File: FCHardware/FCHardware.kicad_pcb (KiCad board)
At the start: 2 copper layers, 39 parts, among them J1 JST-8pin, J3 USB_C_Receptacle_USB2.0_16P, SW3 SW_Push, U2 MPU-6050, U4 TPSM63603, U8 ESP32-S3-MINI-1U, U9 USBLC6-2SC6

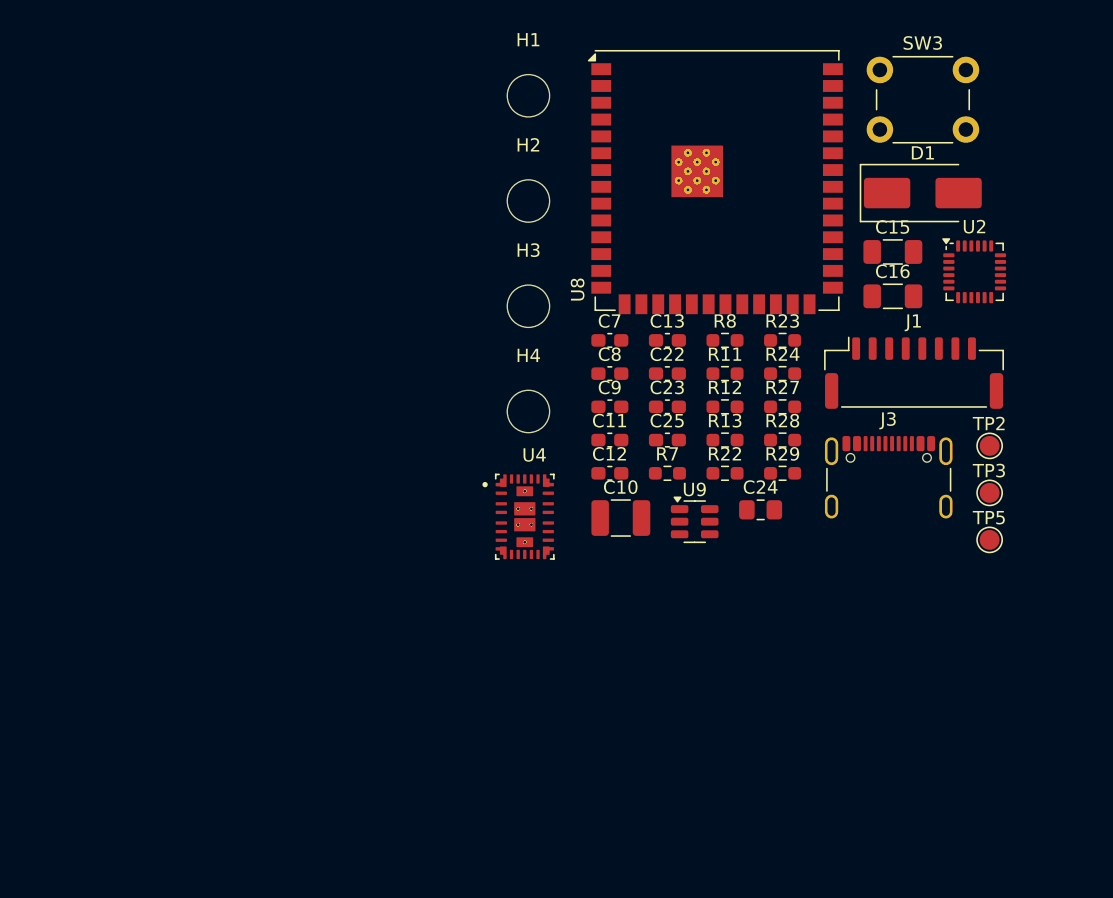
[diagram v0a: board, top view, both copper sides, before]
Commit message: Created basic component placement
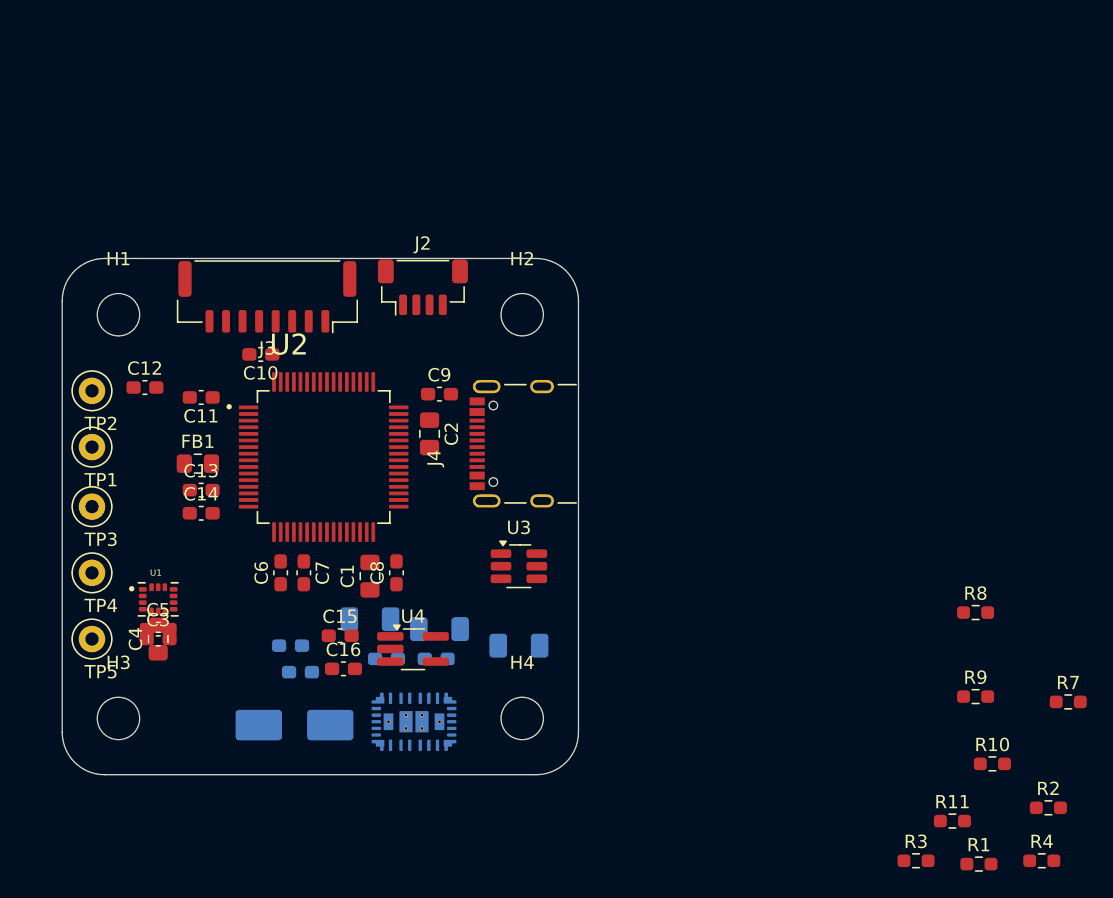
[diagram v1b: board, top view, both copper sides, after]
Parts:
- removed C24: 10u, Capacitor_SMD:C_0805_2012Metric_Pad1.18x1.45mm_HandSolder
- removed C25: 100n, Capacitor_SMD:C_0603_1608Metric_Pad1.08x0.95mm_HandSolder
- removed J1: JST-8pin, Connector_JST:JST_GH_SM08B-GHS-TB_1x08-1MP_P1.25mm_Horizontal
- removed R12: 23.2k, Resistor_SMD:R_0603_1608Metric_Pad0.98x0.95mm_HandSolder
- removed R13, R24, R27: 10k, Resistor_SMD:R_0603_1608Metric_Pad0.98x0.95mm_HandSolder
- removed R22: 510k, Resistor_SMD:R_0603_1608Metric_Pad0.98x0.95mm_HandSolder
- removed R23: 68k, Resistor_SMD:R_0603_1608Metric_Pad0.98x0.95mm_HandSolder
- removed R28, R29: 5k1 +-5%, Resistor_SMD:R_0603_1608Metric_Pad0.98x0.95mm_HandSolder
- removed SW3: SW_Push, Button_Switch_THT:SW_PUSH_6mm
- removed U8: ESP32-S3-MINI-1U, RF_Module:ESP32-S3-WROOM-1U
- removed U9: USBLC6-2SC6, Package_TO_SOT_SMD:SOT-23-6
- added C1: 2u2, Capacitor_SMD:C_0805_2012Metric_Pad1.18x1.45mm_HandSolder, F.Cu at (103.5, 104.2)
- added C14: 1u, Capacitor_SMD:C_0603_1608Metric_Pad1.08x0.95mm_HandSolder, F.Cu at (90.8, 99.5)
- added C17: 680n, Capacitor_SMD:C_0603_1608Metric_Pad1.08x0.95mm_HandSolder, B.Cu at (98.2, 111.5)
- added C18: 100n, Capacitor_SMD:C_0603_1608Metric_Pad1.08x0.95mm_HandSolder, B.Cu at (97.5, 109.5)
- added C19: 22u, Capacitor_SMD:C_1206_3216Metric_Pad1.33x1.80mm_HandSolder, B.Cu at (103.5, 107.5)
- added C2: 2u2, Capacitor_SMD:C_0805_2012Metric_Pad1.18x1.45mm_HandSolder, F.Cu at (108.0, 93.5)
- added C20: 1u, Capacitor_SMD:C_0603_1608Metric_Pad1.08x0.95mm_HandSolder, B.Cu at (104.8, 110.5)
- added C21: 22u, Capacitor_SMD:C_1206_3216Metric_Pad1.33x1.80mm_HandSolder, B.Cu at (108.8, 108.2)
- added C3: 0u1, Capacitor_SMD:C_0603_1608Metric_Pad1.08x0.95mm_HandSolder, F.Cu at (87.5, 109.0)
- added C4: 2u2, Capacitor_SMD:C_0805_2012Metric_Pad1.18x1.45mm_HandSolder, F.Cu at (87.5, 109.0)
- added C5: 0u1, Capacitor_SMD:C_0603_1608Metric_Pad1.08x0.95mm_HandSolder, F.Cu at (87.5, 108.2)
- added C6: 100n, Capacitor_SMD:C_0603_1608Metric_Pad1.08x0.95mm_HandSolder, F.Cu at (96.8, 104.0)
- added FB1: 1kOhm 100Mhz, Inductor_SMD:L_0805_2012Metric_Pad1.15x1.40mm_HandSolder, F.Cu at (90.5, 95.8)
- added J2: JST-4pin, Connector_JST:JST_SH_BM04B-SRSS-TB_1x04-1MP_P1.00mm_Vertical, F.Cu at (107.5, 82.4)
- added J4: UJ20-C-H-G-SMT-2A-P16-TR, FCFootprints:SAMESKY_UJ20-C-H-G-SMT-2A-P16-TR, F.Cu at (116.5, 94.2)
- added R1: 68k, Resistor_SMD:R_0603_1608Metric_Pad0.98x0.95mm_HandSolder, F.Cu at (149.5, 126.0)
- added R10: 5k1, Resistor_SMD:R_0603_1608Metric_Pad0.98x0.95mm_HandSolder, F.Cu at (150.5, 118.4)
- added R2: 510k, Resistor_SMD:R_0603_1608Metric_Pad0.98x0.95mm_HandSolder, F.Cu at (154.8, 121.8)
- added R3: 10k, Resistor_SMD:R_0603_1608Metric_Pad0.98x0.95mm_HandSolder, F.Cu at (144.8, 125.8)
- added R4: 10k, Resistor_SMD:R_0603_1608Metric_Pad0.98x0.95mm_HandSolder, F.Cu at (154.2, 125.8)
- added R9: 10k, Resistor_SMD:R_0603_1608Metric_Pad0.98x0.95mm_HandSolder, F.Cu at (149.2, 113.3)
- added TP1: BootTestPoint, TestPoint:TestPoint_Loop_D1.80mm_Drill1.0mm_Beaded, F.Cu at (82.5, 94.5)
- added TP4: 5VTestPoint, TestPoint:TestPoint_Loop_D1.80mm_Drill1.0mm_Beaded, F.Cu at (82.5, 104.0)
- added U1: ICM-42688-P, FCFootprints:PQFN50P300X250X97-14N, F.Cu at (87.5, 106.0)
- added U3: USBLC6-2SC6, Package_TO_SOT_SMD:SOT-23-6_Handsoldering, F.Cu at (114.8, 103.5)
- added U5: TPSM63603, FCFootprints:CONV_TPSM63603EXTRDHR, B.Cu at (106.8, 115.2)
- C10: value 680n -> 100n; footprint Capacitor_SMD:C_1210_3225Metric_Pad1.33x2.70mm_HandSolder -> Capacitor_SMD:C_0603_1608Metric_Pad1.08x0.95mm_HandSolder
- C12, C7: value 1u -> 100n
- C13: value 100n -> 10n
- C15, C16: value 22u -> 1u; footprint Capacitor_SMD:C_1206_3216Metric_Pad1.33x1.80mm_HandSolder -> Capacitor_SMD:C_0603_1608Metric_Pad1.08x0.95mm_HandSolder
- C22, D1: moved to B.Cu
- C23: value 100n -> 22u; footprint Capacitor_SMD:C_0603_1608Metric_Pad1.08x0.95mm_HandSolder -> Capacitor_SMD:C_1206_3216Metric_Pad1.33x1.80mm_HandSolder; moved to B.Cu
- C9: value 2n2 -> 100n
- J3: value USB_C_Receptacle_USB2.0_16P -> JST-8pin; footprint Connector_USB:USB_C_Receptacle_GCT_USB4105-xx-A_16P_TopMnt_Horizontal -> Connector_Molex:Molex_CLIK-Mate_502386-0870_1x08-1MP_P1.25mm_Horizontal
- R11: value 27.4k -> 5k1
- R7: value 2k2 -> 13k
- R8: value 2k2 -> 40.2k
- TP2: value GNDTestPoint -> ResetTestPoint; footprint TestPoint:TestPoint_Pad_D1.5mm -> TestPoint:TestPoint_Loop_D1.80mm_Drill1.0mm_Beaded
- TP3: value 3V3TestPoint -> GNDTestPoint; footprint TestPoint:TestPoint_Pad_D1.5mm -> TestPoint:TestPoint_Loop_D1.80mm_Drill1.0mm_Beaded
- TP5: value ENTestPoint -> 3V3TestPoint; footprint TestPoint:TestPoint_Pad_D1.5mm -> TestPoint:TestPoint_Loop_D1.80mm_Drill1.0mm_Beaded
- U2: value MPU-6050 -> STM32F405RGTx; footprint Sensor_Motion:InvenSense_QFN-24_4x4mm_P0.5mm -> FCFootprints:QFP50P1200X1200X160-64N
- U4: value TPSM63603 -> AP2112K-3.3; footprint FCFootprints:CONV_TPSM63603EXTRDHR -> Package_TO_SOT_SMD:TSOT-23-5_HandSoldering
- moved TP5 68.2 mm to (82.5, 109.0)
- moved TP2 67.9 mm to (82.5, 90.2)
- moved TP3 67.8 mm to (82.5, 99.0)
- moved D1 62.2 mm to (97.8, 115.5), turned to 180 degrees
- moved U2 51.1 mm to (100.0, 95.2)
- moved C15 50.8 mm to (101.2, 108.8)
- moved C16 50.1 mm to (101.5, 111.2)
- moved J3 49.2 mm to (95.8, 83.2), turned to 180 degrees
- moved H3 43.9 mm to (84.5, 115.0)
- moved R11 37.9 mm to (147.5, 122.8)
- moved C13 37.0 mm to (90.8, 97.8)
- moved C12 35.7 mm to (86.5, 90.0)
- moved H1 35.1 mm to (84.5, 84.5)
- moved R7 34.9 mm to (156.2, 113.8)
- moved C11 31.0 mm to (90.8, 90.8), turned to 180 degrees
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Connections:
- C10 pad 1: GND -> +3V3
- C10 pad 2: VBAT -> GND
- C11 pad 1: GND -> +3V3
- C11 pad 2: VBAT -> GND
- C12 pad 1: GND -> /NRST
- C12 pad 2: Net-(U4-VCC) -> GND
- C13 pad 1: /SW -> GND
- C13 pad 2: Net-(U4-CBOOT) -> /VDD33A
- C15 pad 1: +3V3 -> +5V
- C16 pad 2: VBAT -> +3V3
- C22 pad 1: GND -> /SW
- C23 pad 1: GND -> +5V
- C23 pad 2: Net-(U8-EN) -> GND
- C7 pad 1: Net-(C7-Pad1) -> +3V3
- C7 pad 2: +3V3 -> GND
- C8 pad 1: Net-(C7-Pad1) -> +3V3
- C8 pad 2: Net-(U2-VDD) -> GND
- C9 pad 1: Net-(U2-REGOUT) -> +3V3
- R11 pad 2: Net-(U4-RT) -> Net-(J4-CC2)
- R7 pad 1: +3V3 -> GND
- R7 pad 2: /ACC_SDA -> Net-(U5-RT)
- R8 pad 1: /ACC_SCL -> Net-(U5-FB)
- R8 pad 2: +3V3 -> +5V
- TP2 pad 1: GND -> /NRST
- TP3 pad 1: +3V3 -> GND
- TP5 pad 1: GND -> +3V3
- U2 pad 1: unconnected-(U2-CLKIN-Pad1) -> +3V3
- U2 pad 10: Net-(U2-REGOUT) -> unconnected-(U2-PC2-Pad10)
- U2 pad 11: GND -> unconnected-(U2-PC3-Pad11)
- U2 pad 12: /MPU_INT -> GND
- U2 pad 13: Net-(U2-VDD) -> /VDD33A
- U2 pad 15: unconnected-(U2-NC-Pad15) -> /ESC_CRT
- U2 pad 17: unconnected-(U2-NC-Pad17) -> /V_MON
- U2 pad 19: unconnected-(U2-RESV-Pad19) -> +3V3
- U2 pad 21: unconnected-(U2-RESV-Pad21) -> /M1
- U2 pad 22: unconnected-(U2-RESV-Pad22) -> /M2
- U2 pad 23: /ACC_SCL -> /M3
- U2 pad 24: /ACC_SDA -> unconnected-(U2-PC4-Pad24)
- U2 pad 7: unconnected-(U2-AUX_CL-Pad7) -> /NRST
- U2 pad 8: +3V3 -> unconnected-(U2-PC0-Pad8)
- U2 pad 9: GND -> unconnected-(U2-PC1-Pad9)
- U4 pad 1: Net-(U4-RT) -> +5V
- U4 pad 2: VBAT -> GND
- U4 pad 3: VBAT -> +5V
- U4 pad 4: VBAT -> unconnected-(U4-NC-Pad4)
- U4 pad 5: GND -> +3V3
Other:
- board outline added: 39 x 39 mm

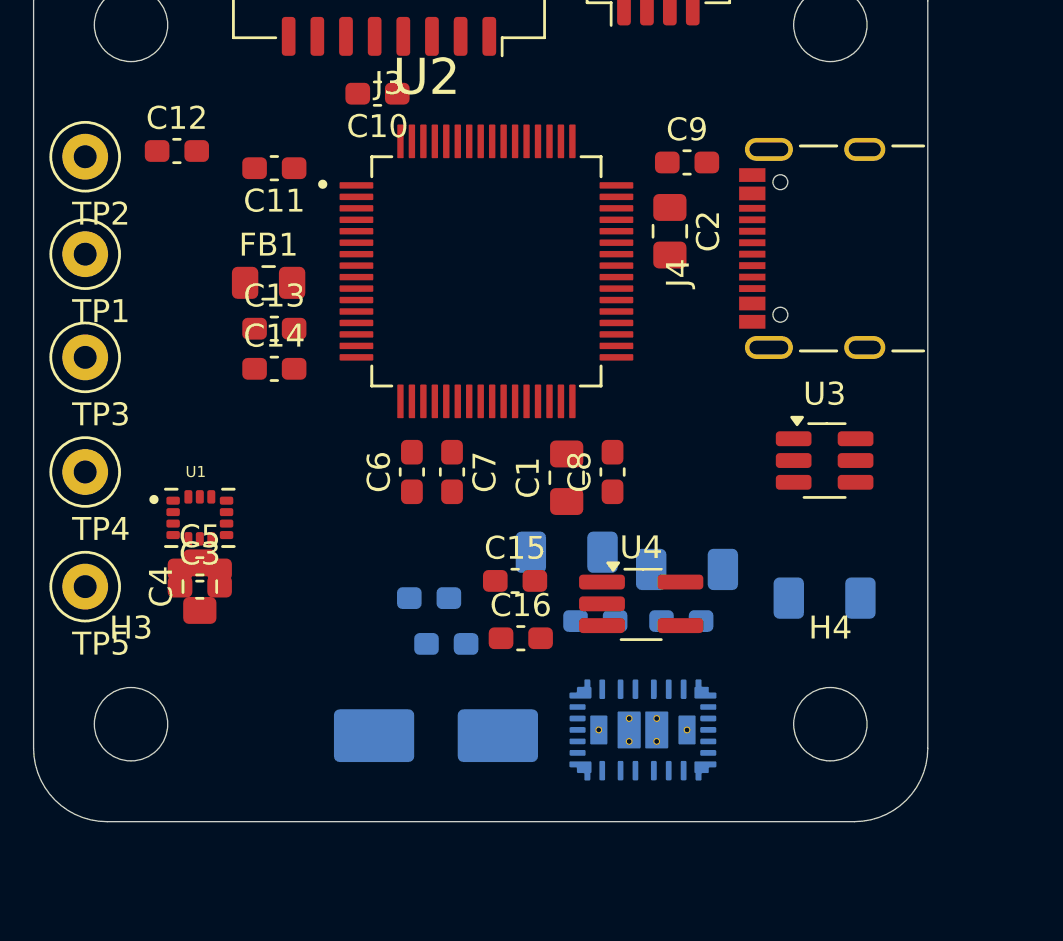
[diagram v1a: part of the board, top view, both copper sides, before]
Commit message: Placed the capacitors
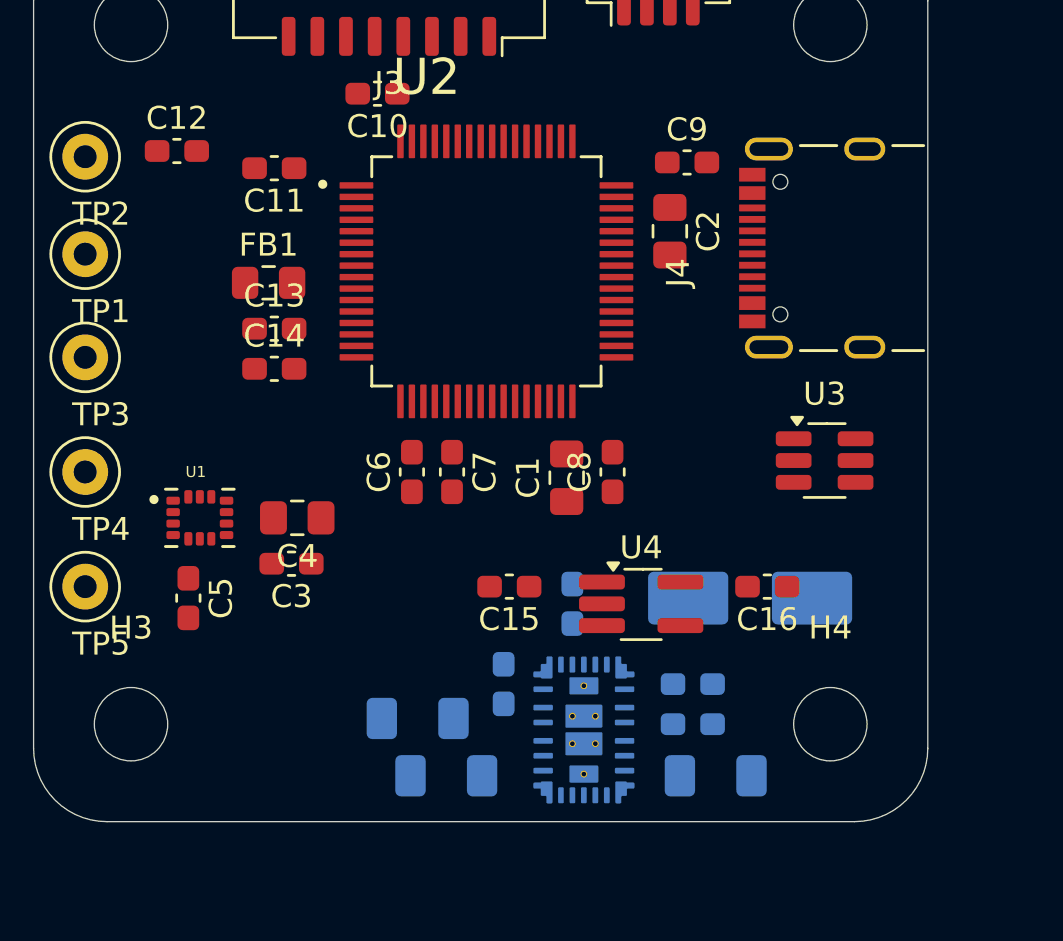
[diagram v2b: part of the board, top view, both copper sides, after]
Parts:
- moved C23 18.5 mm to (97.0, 114.8)
- moved D1 15.0 mm to (111.5, 109.5)
- moved C21 13.8 mm to (98.2, 117.2)
- moved C18 12.7 mm to (109.0, 115.0)
- moved C19 11.7 mm to (110.0, 117.2)
- moved C16 11.0 mm to (112.2, 109.0), turned to 180 degrees
- moved C17 10.9 mm to (109.0, 113.2)
- moved C22 8.22 mm to (100.8, 113.2), turned to -90 degrees
- moved C4 5.20 mm to (91.8, 106.0), turned to 180 degrees
- moved C3 4.12 mm to (91.5, 108.0), turned to 180 degrees
- moved U5 2.58 mm to (104.2, 115.2), turned to 180 degrees
- moved C5 1.35 mm to (87.0, 109.5), turned to -90 degrees
- moved C20 1.25 mm to (103.8, 109.8), turned to -90 degrees
- moved C15 0.35 mm to (101.0, 109.0), turned to 180 degrees

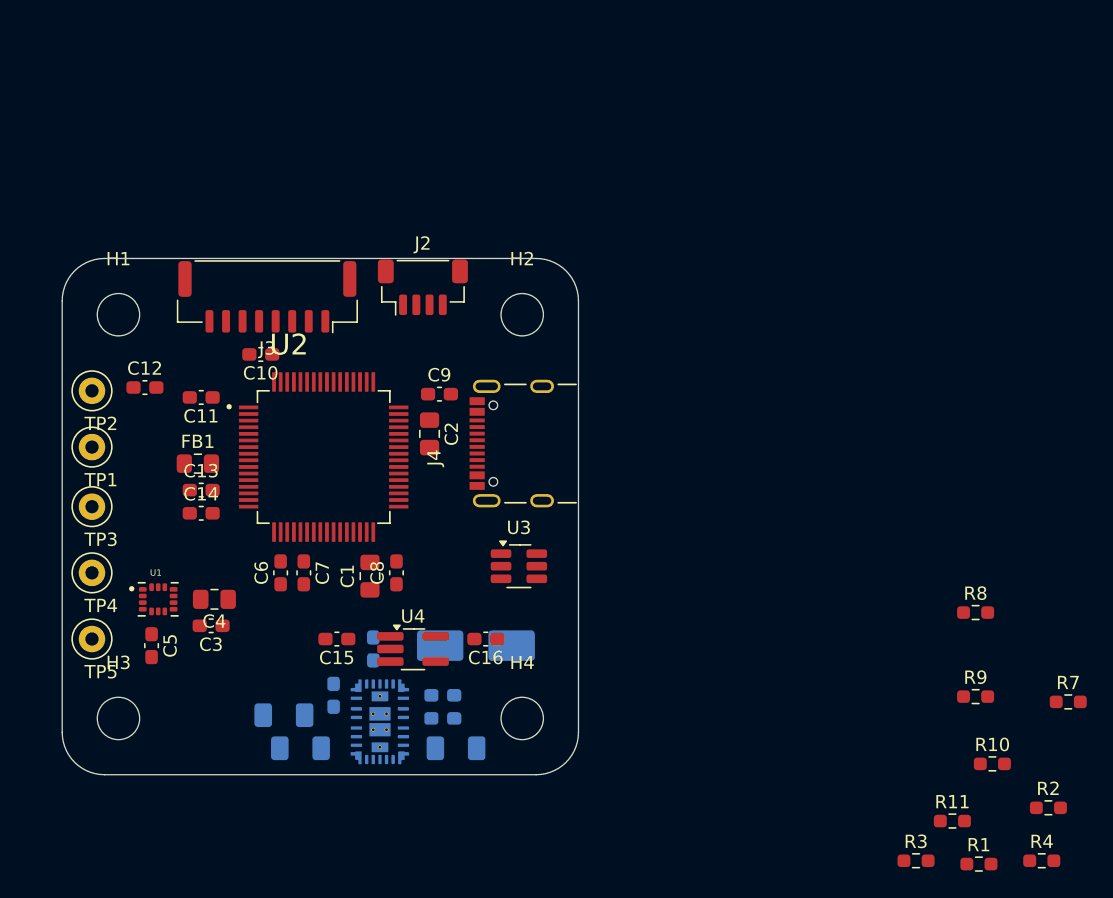
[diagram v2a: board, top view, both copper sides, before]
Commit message: Provisionally placed resistors
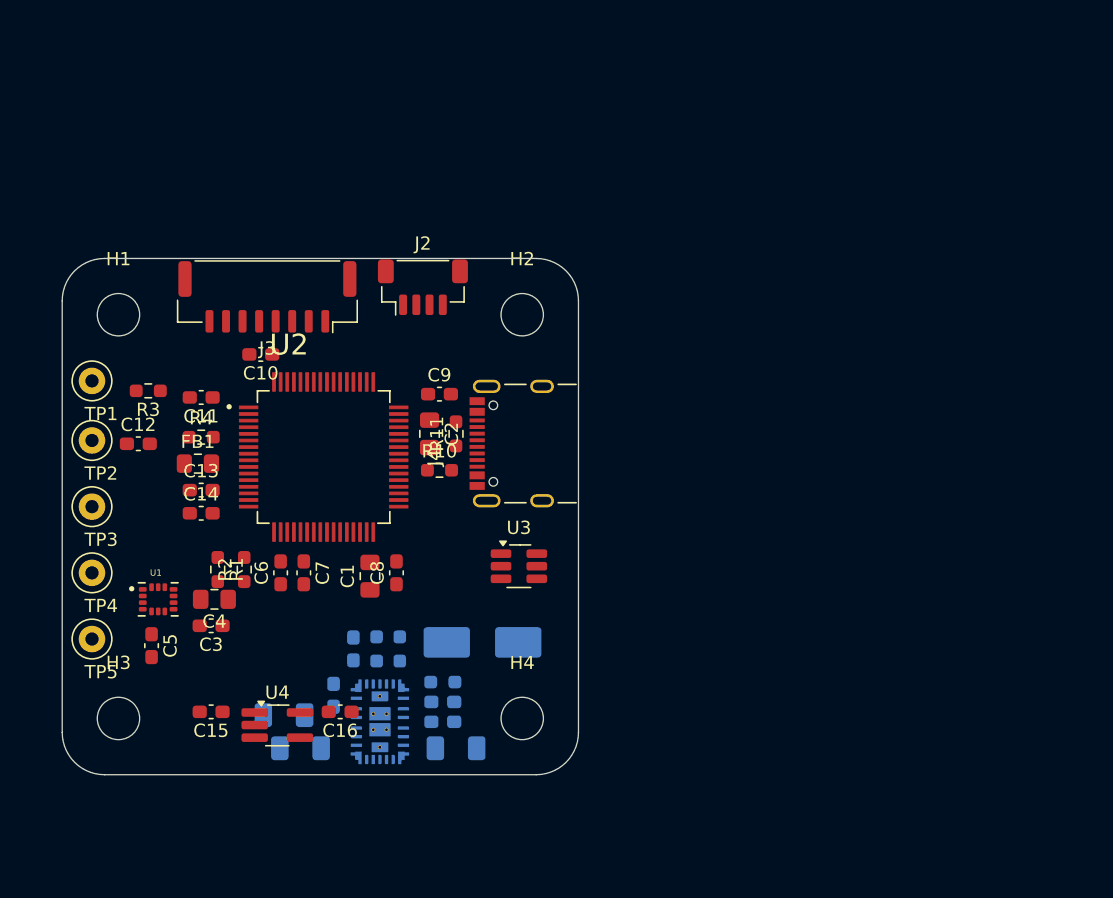
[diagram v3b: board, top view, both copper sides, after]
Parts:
- R7, R8, R9: moved to B.Cu
- moved R4 71.1 mm to (90.8, 93.8)
- moved R3 68.0 mm to (86.8, 90.2), turned to 180 degrees
- moved R2 63.4 mm to (94.0, 103.8), turned to 90 degrees
- moved R1 61.7 mm to (92.0, 103.8), turned to -90 degrees
- moved R11 47.6 mm to (110.0, 93.5), turned to 90 degrees
- moved R10 47.3 mm to (108.8, 96.2)
- moved R7 47.3 mm to (109.0, 112.2), turned to 180 degrees
- moved R8 45.3 mm to (104.0, 109.8), turned to 90 degrees
- moved R9 43.6 mm to (105.8, 109.8), turned to 90 degrees
- moved C16 12.3 mm to (101.2, 114.5)
- moved U4 11.8 mm to (96.5, 115.5)
- moved C15 11.0 mm to (91.5, 114.5)
- moved TP1 5.00 mm to (82.5, 89.5)
- moved C12 4.28 mm to (86.0, 94.2)
- moved TP2 3.75 mm to (82.5, 94.0)
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
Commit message: Provisional routing of TPSM63603
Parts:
- moved C16 16.3 mm to (116.5, 108.8)
- moved C15 15.9 mm to (106.2, 108.5)
- moved U4 15.9 mm to (111.2, 109.5)
- moved R7 4.96 mm to (105.2, 109.0), turned to -90 degrees
- moved C23 4.00 mm to (93.0, 114.7)
- moved C21 3.50 mm to (94.8, 117.2)
- moved C22 2.46 mm to (98.5, 112.2)
- moved C20 2.37 mm to (100.0, 109.0)
- moved R8 2.37 mm to (101.8, 109.0)
- moved R9 2.37 mm to (103.5, 109.0)
- moved U5 2.37 mm to (102.0, 114.5)
- moved C19 1.25 mm to (109.0, 116.5)
- moved C17 0.75 mm to (109.0, 113.0)
- moved C18 0.75 mm to (109.0, 114.5)
- moved D1 0.75 mm to (112.0, 108.5)
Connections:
- U5 pad 18: /VIN -> VBAT
- U5 pad 19: /VIN -> VBAT
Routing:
- net GND: track 0.00 -> 102.4 mm, vias 0 -> 1
- net VBAT: track 0.00 -> 39.5 mm, vias 0 -> 1
- net +5V: track 0.00 -> 37.9 mm
- net /SW: track 0.00 -> 15.1 mm, vias 0 -> 2
- net Net-(U5-FB): track 0.00 -> 3.40 mm
- net Net-(U5-RT): track 0.00 -> 2.93 mm
- net Net-(U5-VCC): track 0.00 -> 2.62 mm
- net Net-(U5-CBOOT): track 0.00 -> 1.89 mm
